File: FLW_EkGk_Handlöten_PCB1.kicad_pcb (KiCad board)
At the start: 2 copper layers, 120 x 66 mm, 112 parts, among them IC60 HCF4094YM013TR, IC61 HCF4094YM013TR, J10 Conn_01x02, J11 Conn_01x02, J12 Conn_01x02, J13 Conn_01x02, Q60 2N7002, Q61 2N7002, Q62 2N7002, Q63 2N7002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

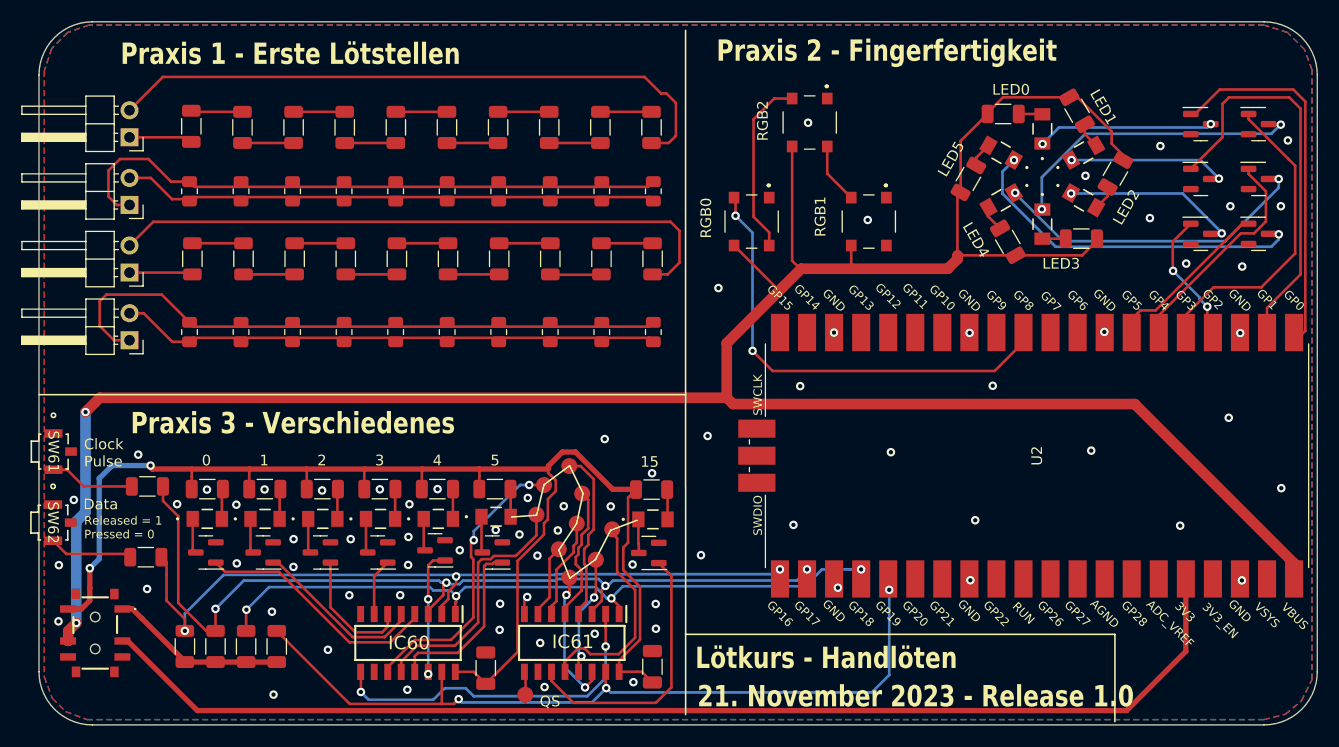
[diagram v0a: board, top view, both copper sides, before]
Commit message: Resolves #1: increased footprint solder mask to get better access with the solder tip
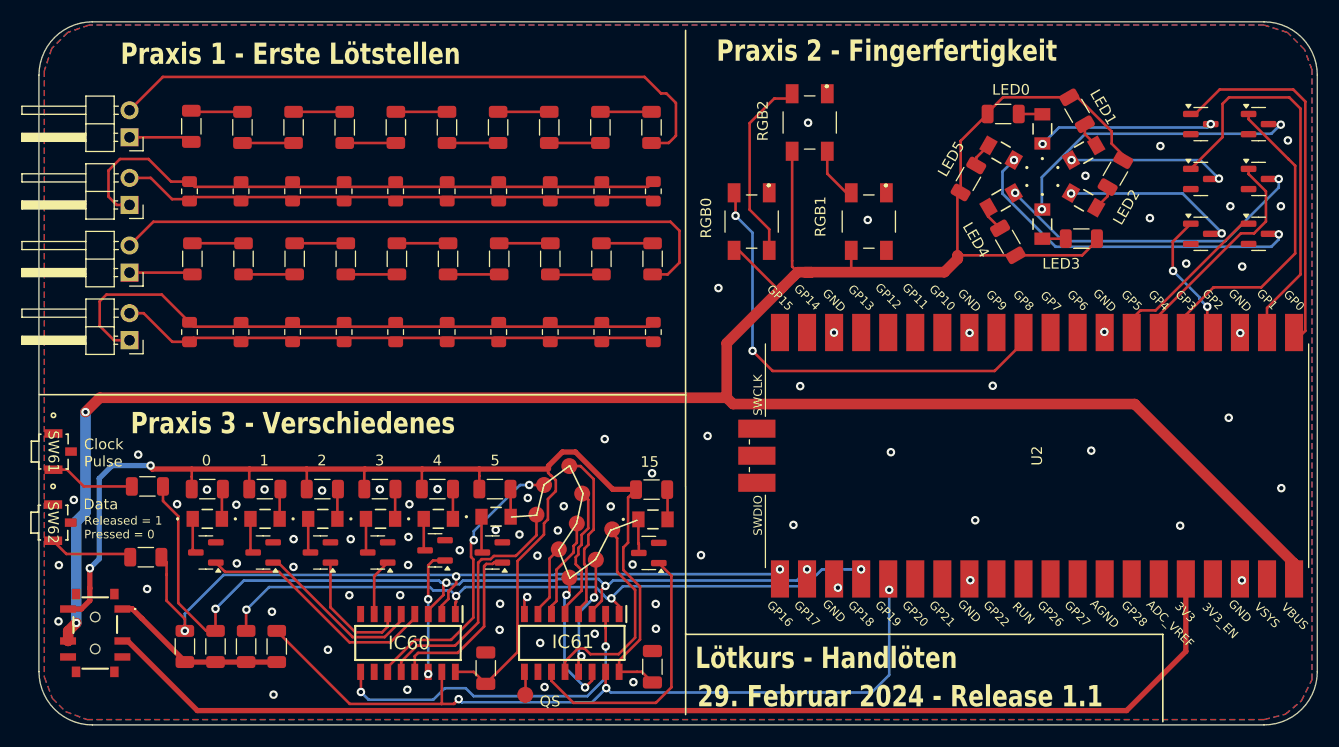
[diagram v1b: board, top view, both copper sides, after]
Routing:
- net /+5V: track 239.3 -> 240.1 mm
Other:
- board text added: "29. Februar 2024 - Release 1.1"
- board text removed: "21. November 2023 - Release 1.0"

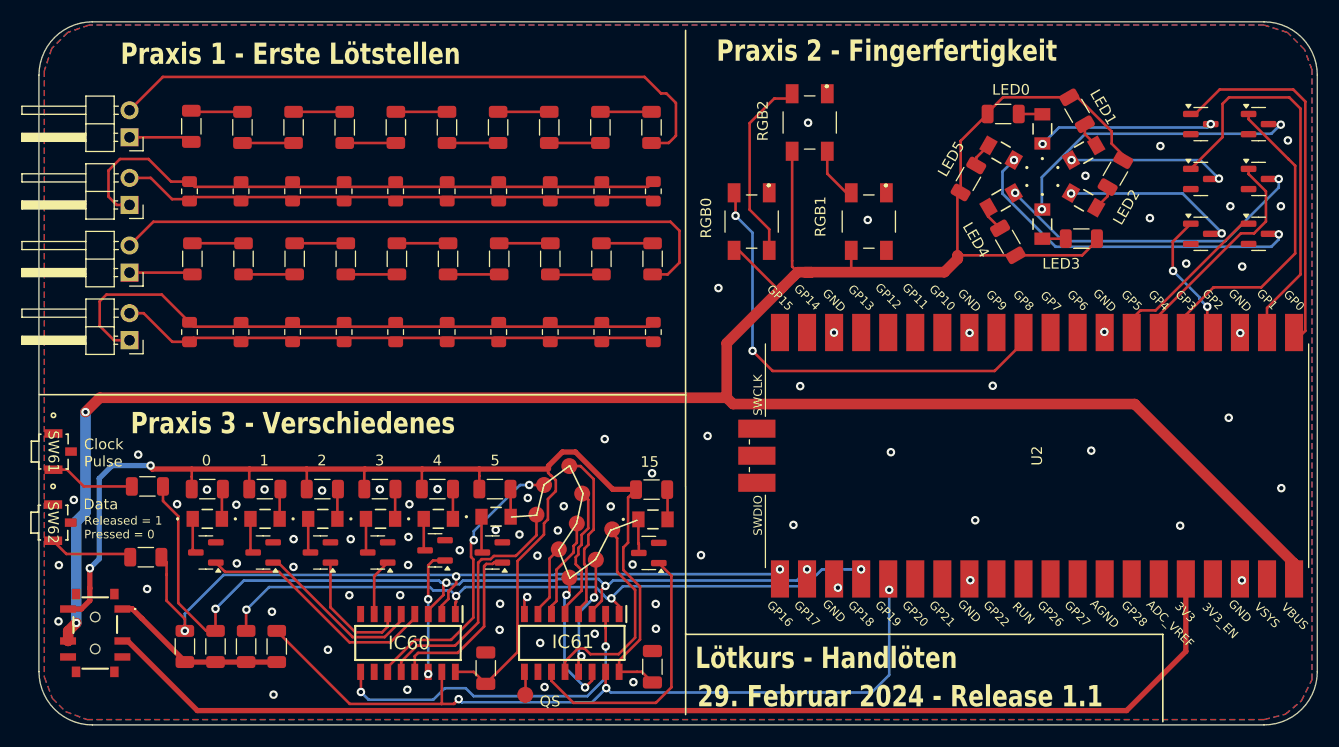
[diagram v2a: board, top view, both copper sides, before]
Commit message: Resolves #3: Missing Pin Marks
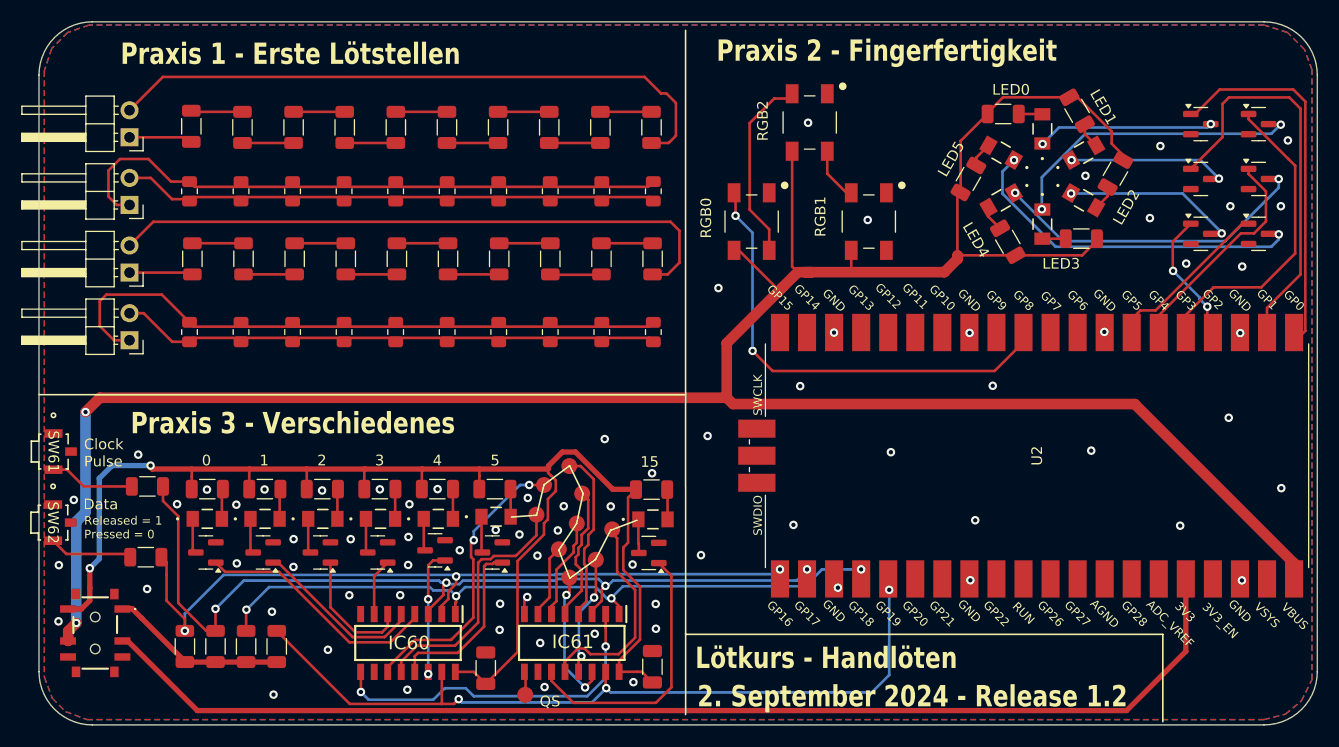
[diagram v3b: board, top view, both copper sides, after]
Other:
- board text added: "2. September 2024 - Release 1.2"
- board text removed: "29. Februar 2024 - Release 1.1"

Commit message: Added C for all digital signals
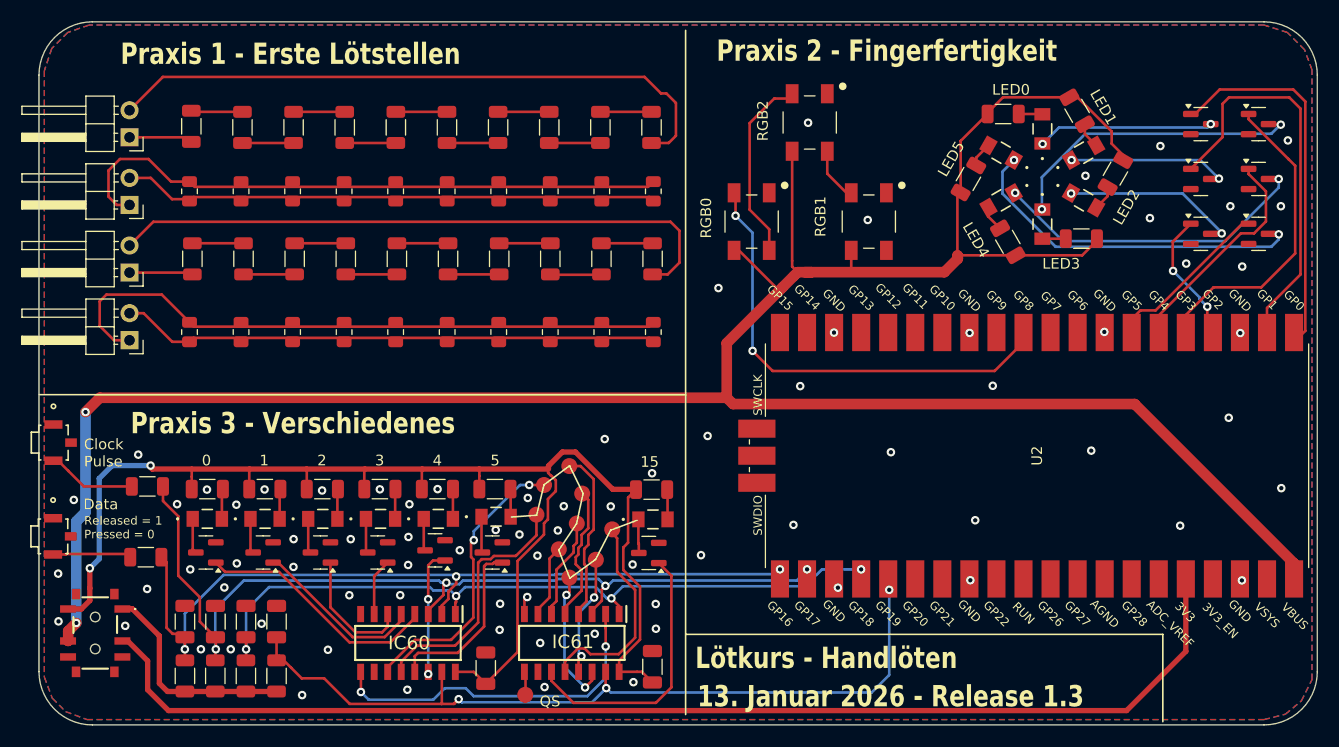
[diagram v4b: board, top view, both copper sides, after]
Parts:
- added C63: 100n, Capacitor_SMD:C_1206_3216Metric, F.Cu at (104.7, 101.3)
- added C64: 100n, Capacitor_SMD:C_1206_3216Metric, F.Cu at (107.6, 101.3)
- added C65: 100n, Capacitor_SMD:C_1206_3216Metric, F.Cu at (110.4, 101.3)
- added C66: 100n, Capacitor_SMD:C_1206_3216Metric, F.Cu at (113.3, 101.3)
- R60, R61, R62, R63, R64, R65, R67, R68, R69, R70, R71, R72, R73: value R -> 620R
- moved R76 2.76 mm to (107.6, 106.4)
- moved R77 2.76 mm to (110.4, 106.4)
- moved R78 2.76 mm to (113.3, 106.4)
- moved R75 2.76 mm to (104.7, 106.4)
- moved SW62 1.29 mm to (92.3, 93.3)
- moved SW61 0.84 mm to (92.4, 84.5)
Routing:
- net /data: track 71.3 -> 76.5 mm
- net /clk: track 83.0 -> 87.2 mm
- net /Praxis 3/+3v3: track 16.6 -> 20.3 mm
- net /strobe: track 66.4 -> 69.9 mm
- net /+3V3: track 112.5 -> 114.1 mm
- net /en: track 74.6 -> 75.8 mm
- net GND: track 1.71 -> 2.49 mm, vias 74 -> 79
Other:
- board text added: "13. Januar 2026 - Release 1.3"
- board text removed: "2. September 2024 - Release 1.2"

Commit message: asdf
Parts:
- removed J10, J11, J12, J13: Conn_01x02, Connector_PinHeader_2.54mm:PinHeader_1x02_P2.54mm_Horizontal
- removed R37: R, Resistor_SMD:R_1206_3216Metric
- removed R47: R, Resistor_SMD:R_0805_2012Metric
- moved R26 15.1 mm to (129.0, 75.1)
- moved R20 15.1 mm to (100.0, 75.1)
- moved R21 15.1 mm to (104.8, 75.1)
- moved R22 15.1 mm to (109.6, 75.1)
- moved R23 15.1 mm to (114.5, 75.1)
- moved R24 15.1 mm to (119.3, 75.1)
- moved R25 15.1 mm to (124.1, 75.1)
- moved R27 15.1 mm to (133.8, 75.1)
- moved R28 15.1 mm to (138.7, 75.1)
- moved R29 15.1 mm to (143.5, 75.1)
- moved R44 8.00 mm to (119.3, 68.0)
- moved R46 8.00 mm to (129.0, 68.0)
- moved R40 8.00 mm to (100.0, 68.0)
- moved R41 8.00 mm to (104.8, 68.0)
- moved R42 8.00 mm to (109.6, 68.0)
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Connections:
- R10 pad 1: Net-(J10-Pin_1) -> Net-(R10-Pad1)
- R19 pad 1: Net-(J10-Pin_2) -> Net-(R10-Pad1)
- R30 pad 1: Net-(J12-Pin_1) -> Net-(R30-Pad1)
- R36 pad 2: Net-(R36-Pad2) -> Net-(R30-Pad1)
- R38 pad 1: Net-(R37-Pad1) -> Net-(R38-Pad1)
- R38 pad 2: Net-(R38-Pad2) -> GND
- R39 pad 1: Net-(J12-Pin_2) -> Net-(R38-Pad1)
- R39 pad 2: Net-(R38-Pad2) -> GND
- R40 pad 1: Net-(J13-Pin_2) -> Net-(R40-Pad1)
- R40 pad 2: Net-(J13-Pin_1) -> Net-(R40-Pad2)
- R41 pad 1: Net-(J13-Pin_2) -> Net-(R40-Pad1)
- R41 pad 2: Net-(J13-Pin_1) -> Net-(R40-Pad2)
- R42 pad 1: Net-(J13-Pin_2) -> Net-(R40-Pad1)
- R42 pad 2: Net-(J13-Pin_1) -> Net-(R40-Pad2)
- R43 pad 1: Net-(J13-Pin_2) -> Net-(R40-Pad1)
- R43 pad 2: Net-(J13-Pin_1) -> Net-(R40-Pad2)
- R44 pad 1: Net-(J13-Pin_2) -> Net-(R40-Pad1)
- R44 pad 2: Net-(J13-Pin_1) -> Net-(R40-Pad2)
- R45 pad 1: Net-(J13-Pin_2) -> Net-(R40-Pad1)
- R45 pad 2: Net-(J13-Pin_1) -> Net-(R40-Pad2)
- R46 pad 1: Net-(J13-Pin_2) -> Net-(R40-Pad1)
- R46 pad 2: Net-(J13-Pin_1) -> Net-(R40-Pad2)
- R48 pad 1: Net-(J13-Pin_2) -> Net-(R48-Pad1)
- R48 pad 2: Net-(J13-Pin_1) -> GND
- R49 pad 1: Net-(J13-Pin_2) -> Net-(R48-Pad1)
- R49 pad 2: Net-(J13-Pin_1) -> GND
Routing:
- net Net-(J13-Pin_1): track 59.3 -> 0.00 mm
- net Net-(R10-Pad1): track 0.00 -> 59.3 mm
- net Net-(J10-Pin_2): track 59.3 -> 0.00 mm
- net Net-(J12-Pin_2): track 58.9 -> 0.00 mm
- net Net-(J13-Pin_2): track 50.6 -> 0.00 mm
- net Net-(R30-Pad1): track 0.00 -> 36.3 mm
- net Net-(R40-Pad2): track 0.00 -> 29.6 mm
- net Net-(R40-Pad1): track 0.00 -> 29.5 mm
- net Net-(R20-Pad2): track 57.6 -> 44.9 mm
- net Net-(R20-Pad1): track 50.4 -> 44.1 mm
- net Net-(R48-Pad1): track 0.00 -> 6.00 mm
- net Net-(R38-Pad1): track 0.00 -> 6.00 mm
- net Net-(J10-Pin_1): track 5.98 -> 0.00 mm
- net Net-(J12-Pin_1): track 5.97 -> 0.00 mm
- net Net-(R37-Pad1): track 4.83 -> 0.00 mm
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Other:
- board text added: "13. Mai 2026 - Release 1.4"
- board text added: "Übermässig wärmeabführend"
- board text removed: "13. Januar 2026 - Release 1.3"
